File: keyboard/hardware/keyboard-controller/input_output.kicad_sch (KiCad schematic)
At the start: 25 parts, among them J4 SYNC_IN, J5 CV_OUT, J6 GATE_OUT, J7 SYNC_OUT, Q1 2N3904, U8 LM358, U9 LM358

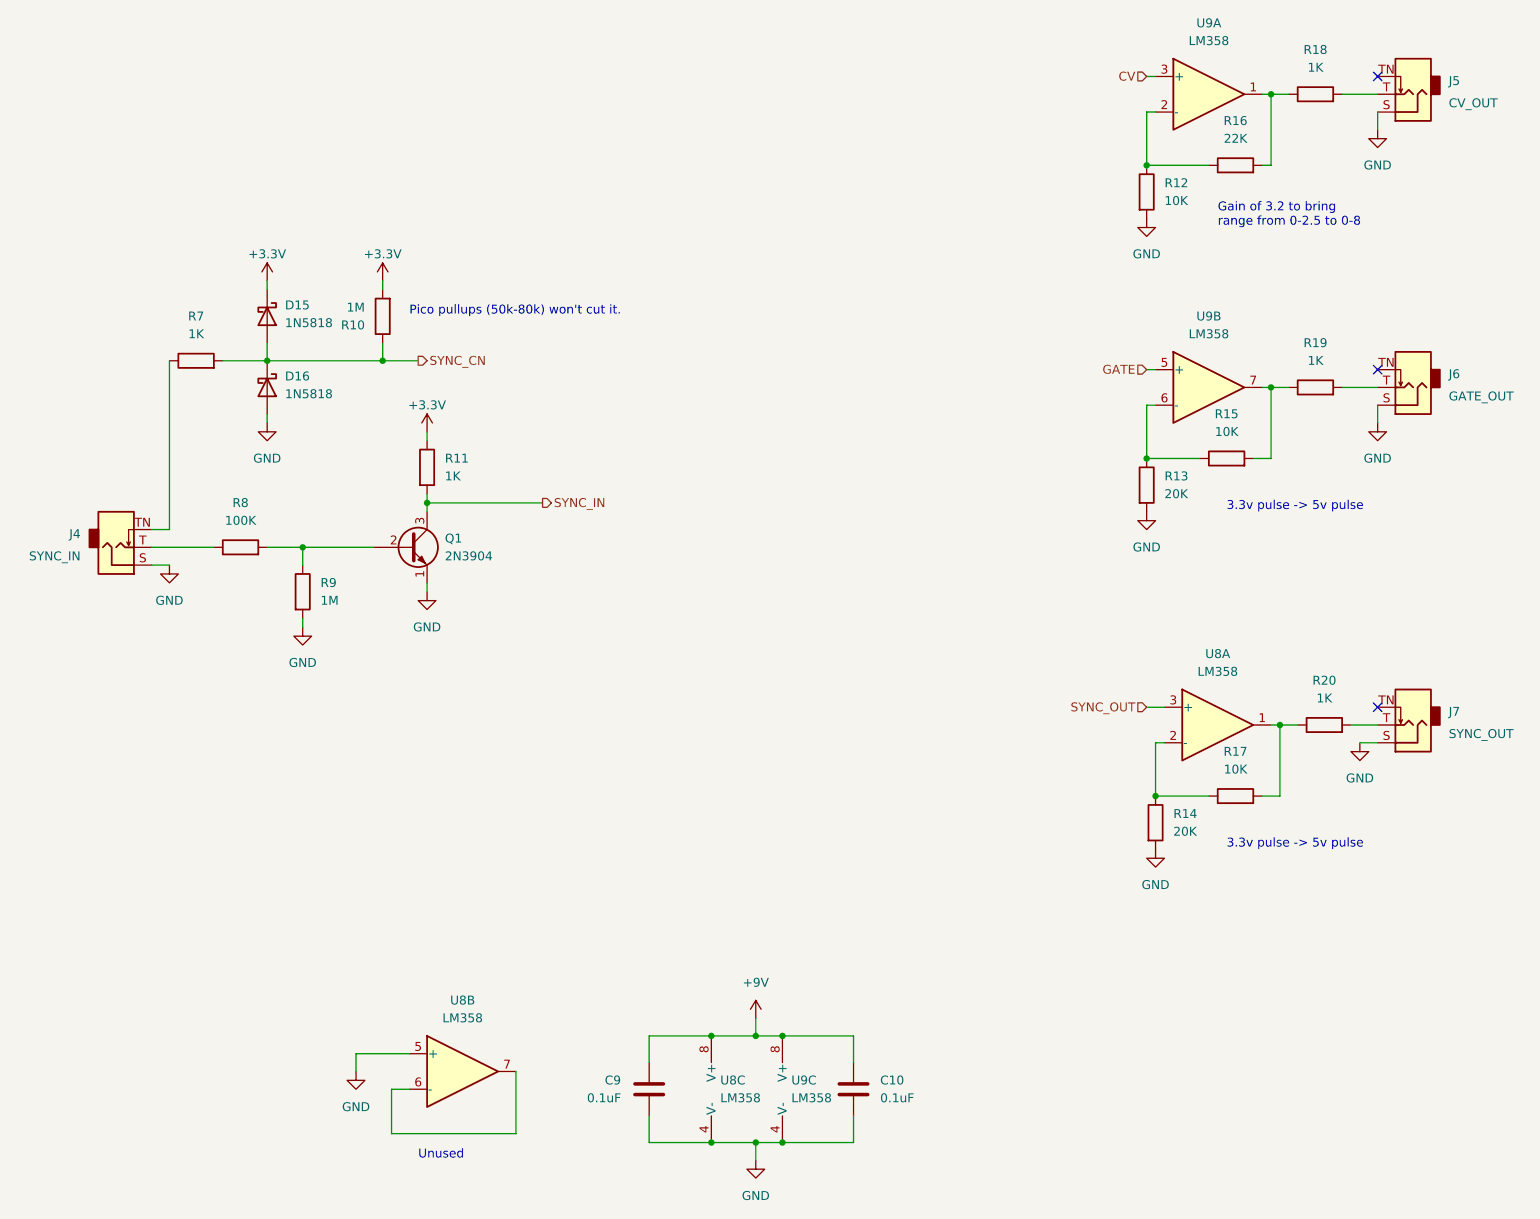
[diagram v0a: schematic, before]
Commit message: Simplified keyboard for rev1
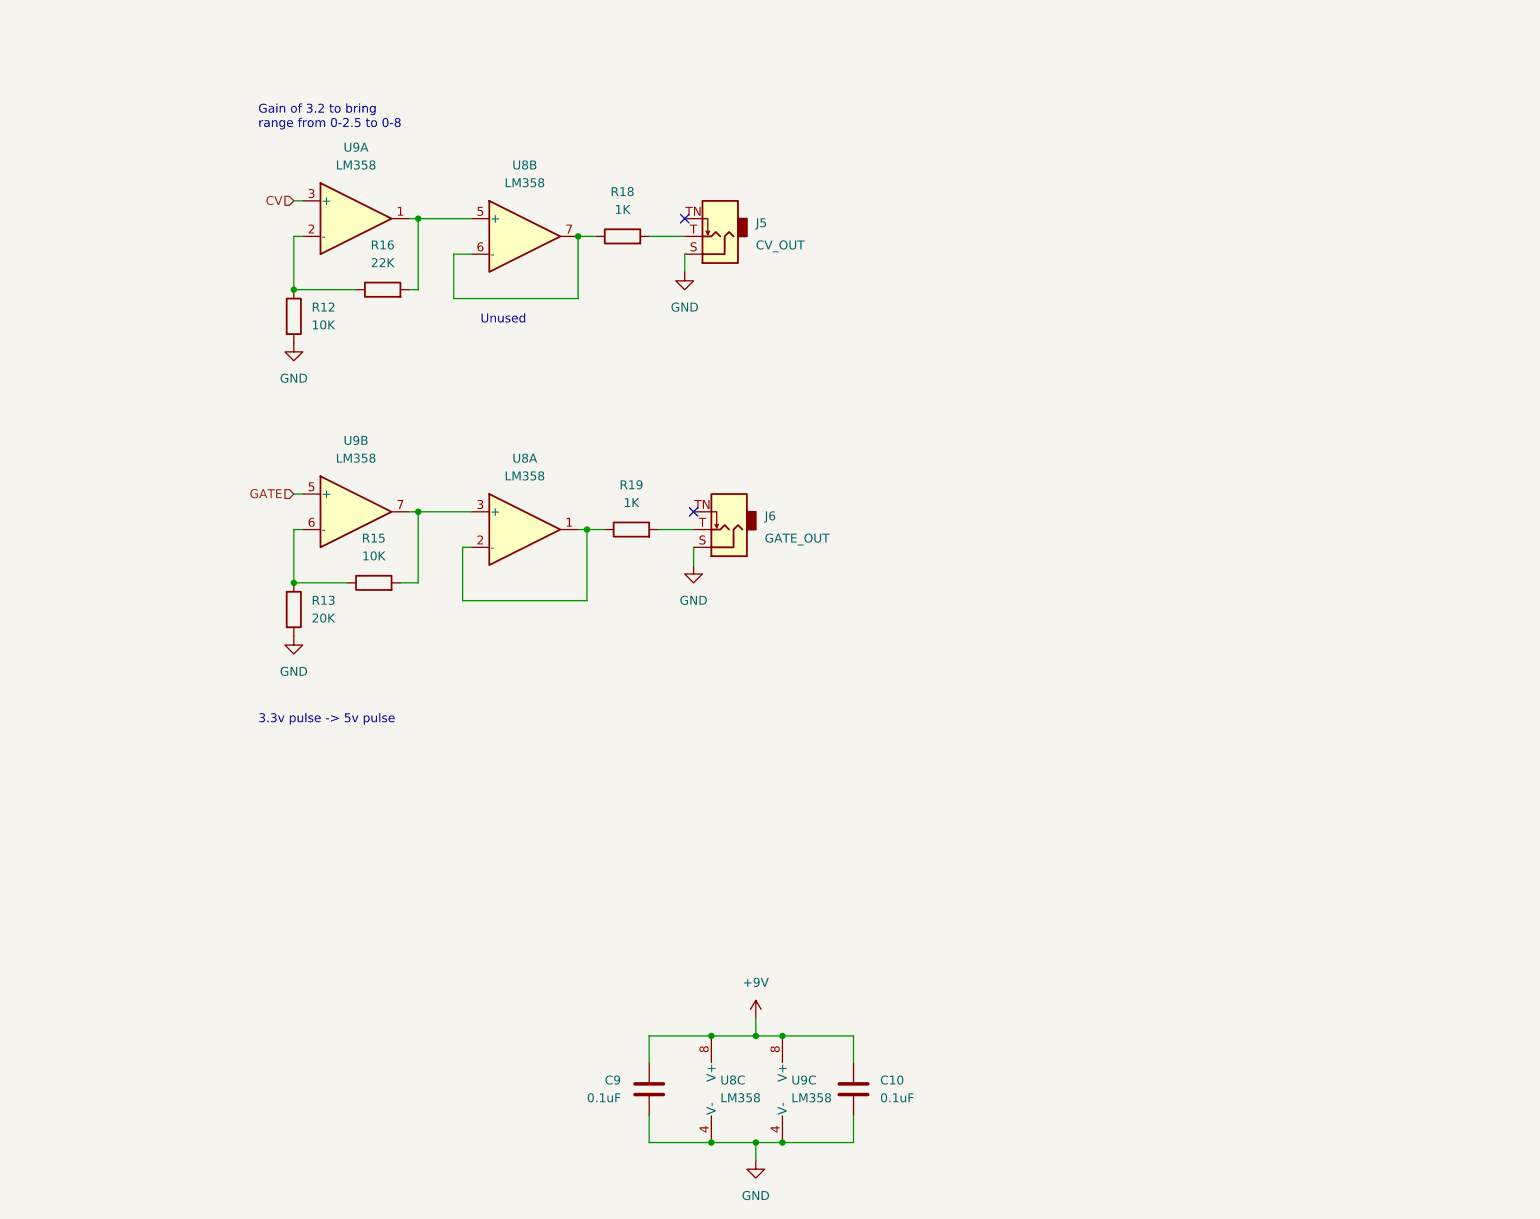
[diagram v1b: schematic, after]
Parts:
- removed D15, D16: 1N5818, Diode_THT:D_DO-41_SOD81_P10.16mm_Horizontal, symbol Diode:1N5818
- removed J4: SYNC_IN, AudioJacks:Jack_3.5mm_QingPu_WQP-PJ398SM_Vertical, symbol Connector:AudioJack2_SwitchT
- removed J7: SYNC_OUT, AudioJacks:Jack_3.5mm_QingPu_WQP-PJ398SM_Vertical, symbol Connector:AudioJack2_SwitchT
- removed Q1: 2N3904, Package_TO_SOT_THT:TO-92_Inline, symbol Transistor_BJT:2N3904
- removed R10, R9: 1M, Royal_Ohm_Resistors:R_Axial_DIN0207_L6.8mm_D2.5mm_P10.16mm_Horizontal, symbol Device:R
- removed R11, R20, R7: 1K, Royal_Ohm_Resistors:R_Axial_DIN0207_L6.8mm_D2.5mm_P10.16mm_Horizontal, symbol Device:R
- removed R14: 20K, Royal_Ohm_Resistors:R_Axial_DIN0207_L6.8mm_D2.5mm_P10.16mm_Horizontal, symbol Device:R
- removed R17: 10K, Royal_Ohm_Resistors:R_Axial_DIN0207_L6.8mm_D2.5mm_P10.16mm_Horizontal, symbol Device:R
- removed R8: 100K, Royal_Ohm_Resistors:R_Axial_DIN0207_L6.8mm_D2.5mm_P10.16mm_Horizontal, symbol Device:R
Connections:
- net SYNC_OUT is gone; now on an unnamed net: U8.3 (+)
- net GND: no longer U8.5 (+)
- net at U8.2 (-): now also R19.1, U8.1
- net at R15.2, U9.7: no longer R19.1
- net at U8.6 (-), U8.7: now also R18.1
- net at R16.2, U9.1: now also U8.5 (+); no longer R18.1
- no-connect marks 3 -> 2
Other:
- note removed: "Pico pullups (50k-80k) won't cut it."
- moved on the sheet: J5, J6, R12, R13, R15, R16, R18, R19, U8A, U8B, U9A, U9B

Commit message: Finalized keyboard controller rev1 board
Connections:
- net GATE: now also U8.5 (+); no longer U9.5 (+)
- net at R16.2, U9.1: now also U9.5 (+); no longer U8.5 (+)
- net at R13.1, R15.1: now also U8.6 (-); no longer U9.6 (-)
- net at R15.2, U8.3 (+): now also U8.7; no longer U9.7
- new net: R18.1, U9.6 (-), U9.7
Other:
- note removed: "Unused"
- moved on the sheet: U8B, U9B

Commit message: Completed keyboard controller rev2
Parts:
- added TP7: CV, TestPoint:TestPoint_Pad_D1.5mm, symbol Connector:TestPoint
- added TP8: Gate, TestPoint:TestPoint_Pad_D1.5mm, symbol Connector:TestPoint
- renumbered J5 to J4, J6 to J5, R18 to R10, R19 to R11, R12 to R6, R13 to R7, R15 to R8, R16 to R9, U9 to U8, U8 to U9
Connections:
- net at J5.T, R11.2: now also TP8.1
- net at J4.T, R10.2: now also TP7.1
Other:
- moved on the sheet: J4, J5
